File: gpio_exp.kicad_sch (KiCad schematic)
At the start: 23 parts, among them U9 PCA9685PW

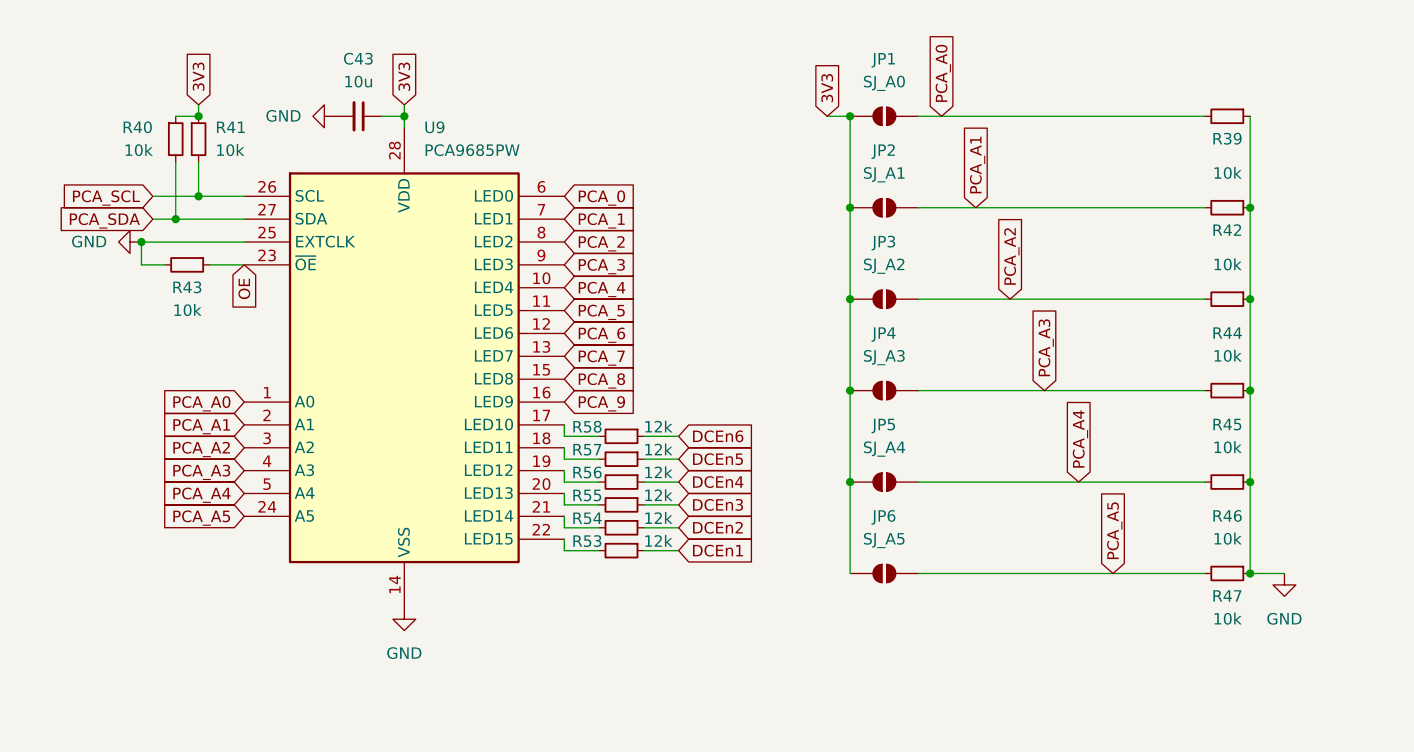
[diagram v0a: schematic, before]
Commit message: gpio expander added comm finished
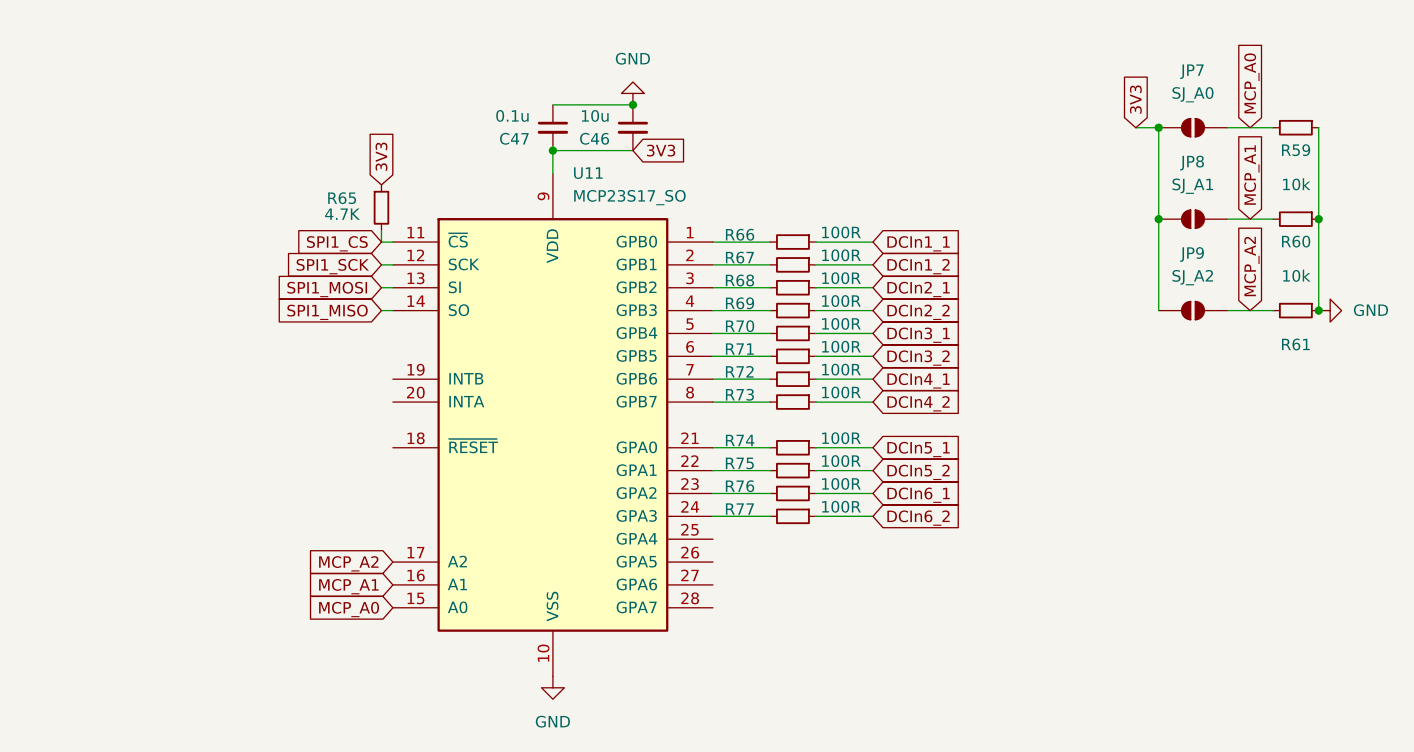
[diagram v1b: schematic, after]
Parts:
- removed C43: 10u, Capacitor_SMD:C_0805_2012Metric, symbol Device:C_Small
- removed JP1: SJ_A0, Jumper:SolderJumper-2_P1.3mm_Open_RoundedPad1.0x1.5mm, symbol Jumper:SolderJumper_2_Open
- removed JP2: SJ_A1, Jumper:SolderJumper-2_P1.3mm_Open_RoundedPad1.0x1.5mm, symbol Jumper:SolderJumper_2_Open
- removed JP3: SJ_A2, Jumper:SolderJumper-2_P1.3mm_Open_RoundedPad1.0x1.5mm, symbol Jumper:SolderJumper_2_Open
- removed JP4: SJ_A3, Jumper:SolderJumper-2_P1.3mm_Open_RoundedPad1.0x1.5mm, symbol Jumper:SolderJumper_2_Open
- removed JP5: SJ_A4, Jumper:SolderJumper-2_P1.3mm_Open_RoundedPad1.0x1.5mm, symbol Jumper:SolderJumper_2_Open
- removed JP6: SJ_A5, Jumper:SolderJumper-2_P1.3mm_Open_RoundedPad1.0x1.5mm, symbol Jumper:SolderJumper_2_Open
- removed R39, R40, R41, R42, R43, R44, R45, R46, R47: 10k, Resistor_SMD:R_0805_2012Metric, symbol Device:R_Small
- removed R53, R54, R55, R56, R57, R58: 12k, Resistor_SMD:R_0805_2012Metric, symbol Device:R_Small
- removed U9: PCA9685PW, Package_SO:TSSOP-28_4.4x9.7mm_P0.65mm, symbol Driver_LED:PCA9685PW
- added C46: 10u, Capacitor_SMD:C_0805_2012Metric, symbol Device:C_Small
- added C47: 0.1u, Capacitor_SMD:C_0805_2012Metric, symbol Device:C_Small
- added JP7: SJ_A0, Jumper:SolderJumper-2_P1.3mm_Open_RoundedPad1.0x1.5mm, symbol Jumper:SolderJumper_2_Open
- added JP8: SJ_A1, Jumper:SolderJumper-2_P1.3mm_Open_RoundedPad1.0x1.5mm, symbol Jumper:SolderJumper_2_Open
- added JP9: SJ_A2, Jumper:SolderJumper-2_P1.3mm_Open_RoundedPad1.0x1.5mm, symbol Jumper:SolderJumper_2_Open
- added R59, R60, R61: 10k, Resistor_SMD:R_0805_2012Metric, symbol Device:R_Small
- added R65: 4.7K, Resistor_SMD:R_0805_2012Metric, symbol Device:R_Small
- added R66, R67, R68, R69, R70, R71, R72, R73, R74, R75, R76, R77: 100R, Resistor_SMD:R_0805_2012Metric, symbol Device:R_Small
- added U11: MCP23S17_SO, Package_SO:SOIC-28W_7.5x17.9mm_P1.27mm, symbol Interface_Expansion:MCP23S17_SO
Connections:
- net 3V3: now also C46.2, C47.2, JP7.1 (A), JP8.1 (A), JP9.1 (A), R65.1, U11.9 (VDD)
- net GND: now also C46.1, C47.1, R59.1, R60.1, R61.1, U11.10 (VSS)
- new net: R73.2, U11.8 (GPB7)
- new net: R70.2, U11.5 (GPB4)
- new net: R66.2, U11.1 (GPB0)
- new net: R67.2, U11.2 (GPB1)
- new net: R74.2, U11.21 (GPA0)
- new net: R75.2, U11.22 (GPA1)
- new net: R76.2, U11.23 (GPA2)
- new net: R77.2, U11.24 (GPA3)
- new net: R68.2, U11.3 (GPB2)
- new net: R69.2, U11.4 (GPB3)
- new net: R71.2, U11.6 (GPB5)
- new net: R72.2, U11.7 (GPB6)
- new net DCIn1_1: R66.1
- new net DCIn1_2: R67.1
- new net DCIn2_1: R68.1
- new net DCIn2_2: R69.1
- new net DCIn3_1: R70.1
- new net DCIn3_2: R71.1
- new net DCIn4_1: R72.1
- new net DCIn4_2: R73.1
- new net DCIn5_1: R74.1
- new net DCIn5_2: R75.1
- new net DCIn6_1: R76.1
- new net DCIn6_2: R77.1
- new net MCP_A0: JP7.2 (B), R59.2, U11.15 (A0)
- new net MCP_A1: JP8.2 (B), R60.2, U11.16 (A1)
- new net MCP_A2: JP9.2 (B), R61.2, U11.17 (A2)
- new net SPI1_CS: R65.2, U11.11 (~{CS})
- new net SPI1_MISO: U11.14 (SO)
- new net SPI1_MOSI: U11.13 (SI)
- new net SPI1_SCK: U11.12 (SCK)

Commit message: Visual Improvements
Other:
- note added: "GPIO Expander"
- note added: "GPIO Expander Address Selection"
- moved on the sheet: C46, C47, JP7, JP8, JP9, R59, R60, R61, R65, R66, R67, R68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

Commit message: schematic finished
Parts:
- added R84: 10K, Resistor_SMD:R_0805_2012Metric, symbol Device:R_Small
- renumbered C47 to C46, C46 to C47, R59 to R68, R65 to R69, R66 to R70, R67 to R71, R60 to R72, R68 to R73, R69 to R74, R70 to R75, R71 to R76, R61 to R77, R72 to R78, R73 to R79, R74 to R80, R75 to R81, R76 to R82, R77 to R83
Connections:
- net 3V3: now also R84.1
- net at U11.18 (~{RESET}): now also R84.2
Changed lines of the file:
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@@
+	(wire
+		(pts
+			(xy 29.21 58.42) (xy 33.02 58.42)
+		)
+		(stroke
+			(width 0)
+			(type default)
+		)
+	)
 	(wire
 		(pts
@@
 		)
 	)
+	(global_label "3V3"
+		(shape input)
+		(at 29.21 53.34 90)
+		(fields_autoplaced yes)
+		(effects
+			(font
+				(size 1.27 1.27)
+			)
+			(justify left)
+		)
+		(property "Intersheetrefs" "${INTERSHEET_REFS}"
+			(at 29.21 46.8472 90)
+			(effects
+				(font
+					(size 1.27 1.27)
+				)
+				(justify left)
+				(hide yes)
+			)
+		)
+	)
 	(global_label "DCIn3_2"
 		(shape input)
@@
 		(on_board yes)
 		(dnp no)
-		(property "Reference" "R73"
+		(property "Reference" "R79"
 			(at 69.85 52.578 90)
 			(effects
@@
 			(project "controllerForVehicle"
 				(path "/f177fb06-71dc-4865-9331-a828b12c2bf7/cf99d41f-154f-4525-9df8-a364b4903864"
-					(reference "R73")
+					(reference "R79")
 					(unit 1)
 				)
@@
 		(on_board yes)
 		(dnp no)
-		(property "Reference" "R70"
+		(property "Reference" "R75"
 			(at 69.85 44.958 90)
 			(effects
@@
 			(project "controllerForVehicle"
 				(path "/f177fb06-71dc-4865-9331-a828b12c2bf7/cf99d41f-154f-4525-9df8-a364b4903864"
-					(reference "R70")
+					(reference "R75")
 					(unit 1)
 				)
@@
 		(dnp no)
 		(fields_autoplaced yes)
-		(property "Reference" "#PWR050"
+		(property "Reference" "#PWR051"
 			(at 50.8 90.17 0)
 			(effects
@@
 			(project "controllerForVehicle"
 				(path "/f177fb06-71dc-4865-9331-a828b12c2bf7/cf99d41f-154f-4525-9df8-a364b4903864"
-					(reference "#PWR050")
+					(reference "#PWR051")
 					(unit 1)
 				)
@@
 		(on_board yes)
 		(dnp no)
-		(property "Reference" "R77"
+		(property "Reference" "R83"
 			(at 69.85 65.278 90)
 			(effects
@@
 			(project "controllerForVehicle"
 				(path "/f177fb06-71dc-4865-9331-a828b12c2bf7/cf99d41f-154f-4525-9df8-a364b4903864"
-					(reference "R77")
+					(reference "R83")
 					(unit 1)
 				)
@@
 		(dnp no)
 		(fields_autoplaced yes)
-		(property "Reference" "C47"
+		(property "Reference" "C46"
 			(at 48.26 24.1365 0)
 			(effects
@@
 			(project "controllerForVehicle"
 				(path "/f177fb06-71dc-4865-9331-a828b12c2bf7/cf99d41f-154f-4525-9df8-a364b4903864"
-					(reference "C47")
+					(reference "C46")
 					(unit 1)
 				)
@@
 		(dnp no)
 		(fields_autoplaced yes)
-		(property "Reference" "C46"
+		(property "Reference" "C47"
 			(at 57.15 24.1365 0)
 			(effects
@@
 			(project "controllerForVehicle"
 				(path "/f177fb06-71dc-4865-9331-a828b12c2bf7/cf99d41f-154f-4525-9df8-a364b4903864"
-					(reference "C46")
+					(reference "C47")
 					(unit 1)
 				)
@@
 		(on_board yes)
 		(dnp no)
-		(property "Reference" "R75"
+		(property "Reference" "R81"
 			(at 69.8482 60.198 90)
 			(effects
@@
 			(project "controllerForVehicle"
 				(path "/f177fb06-71dc-4865-9331-a828b12c2bf7/cf99d41f-154f-4525-9df8-a364b4903864"
-					(reference "R75")
+					(reference "R81")
 					(unit 1)
 				)
@@
 		(on_board yes)
 		(dnp no)
-		(property "Reference" "R68"
+		(property "Reference" "R73"
 			(at 69.85 39.878 90)
 			(effects
@@
 			(project "controllerForVehicle"
 				(path "/f177fb06-71dc-4865-9331-a828b12c2bf7/cf99d41f-154f-4525-9df8-a364b4903864"
-					(reference "R68")
+					(reference "R73")
 					(unit 1)
 				)
@@
 		(on_board yes)
 		(dnp no)
-		(property "Reference" "R74"
+		(property "Reference" "R80"
 			(at 69.85 57.658 90)
 			(effects
@@
 			(project "controllerForVehicle"
 				(path "/f177fb06-71dc-4865-9331-a828b12c2bf7/cf99d41f-154f-4525-9df8-a364b4903864"
-					(reference "R74")
+					(reference "R80")
 					(unit 1)
 				)
@@
 		(on_board yes)
 		(dnp no)
-		(property "Reference" "R72"
+		(property "Reference" "R78"
 			(at 69.85 50.038 90)
 			(effects
@@
 			(project "controllerForVehicle"
 				(path "/f177fb06-71dc-4865-9331-a828b12c2bf7/cf99d41f-154f-4525-9df8-a364b4903864"
-					(reference "R72")
+					(reference "R78")
 					(unit 1)
 				)
@@
 		(on_board yes)
 		(dnp no)
-		(property "Reference" "R71"
+		(property "Reference" "R76"
 			(at 69.85 47.498 90)
 			(effects
@@
 			(project "controllerForVehicle"
 				(path "/f177fb06-71dc-4865-9331-a828b12c2bf7/cf99d41f-154f-4525-9df8-a364b4903864"
-					(reference "R71")
+					(reference "R76")
 					(unit 1)
 				)
@@
 		(on_board yes)
 		(dnp no)
-		(property "Reference" "R61"
+		(property "Reference" "R77"
 			(at 133.35 53.34 90)
 			(effects
@@
 			(project "controllerForVehicle"
 				(path "/f177fb06-71dc-4865-9331-a828b12c2bf7/cf99d41f-154f-4525-9df8-a364b4903864"
-					(reference "R61")
+					(reference "R77")
+					(unit 1)
+				)
+			)
+		)
+	)
+	(symbol
+		(lib_id "Device:R_Small")
+		(at 29.21 55.88 0)
+		(unit 1)
+		(exclude_from_sim no)
+		(in_bom yes)
+		(on_board yes)
+		(dnp no)
+		(property "Reference" "R84"
+			(at 23.114 54.864 0)
+			(effects
+				(font
+					(size 1.27 1.27)
+				)
+				(justify left)
+			)
+		)
+		(property "Value" "10K"
+			(at 23.368 56.896 0)
+			(effects
+				(font
+					(size 1.27 1.27)
+				)
+				(justify left)
+			)
+		)
+		(property "Footprint" "Resistor_SMD:R_0805_2012Metric"
+			(at 29.21 55.88 0)
+			(effects
+				(font
+					(size 1.27 1.27)
+				)
+				(hide yes)
+			)
+		)
+		(property "Datasheet" "~"
+			(at 29.21 55.88 0)
+			(effects
+				(font
+					(size 1.27 1.27)
+				)
+				(hide yes)
+			)
+		)
+		(property "Description" "Resistor, small symbol"
+			(at 29.21 55.88 0)
+			(effects
+				(font
+					(size 1.27 1.27)
+				)
+				(hide yes)
+			)
+		)
+		(pin "1"
+		)
+		(pin "2"
+		)
+		(instances
+			(project "controllerForVehicle"
+				(path "/f177fb06-71dc-4865-9331-a828b12c2bf7/cf99d41f-154f-4525-9df8-a364b4903864"
+					(reference "R84")
 					(unit 1)
 				)
@@
 		(on_board yes)
 		(dnp no)
-		(property "Reference" "R76"
+		(property "Reference" "R82"
 			(at 69.8482 62.738 90)
 			(effects
@@
 			(project "controllerForVehicle"
 				(path "/f177fb06-71dc-4865-9331-a828b12c2bf7/cf99d41f-154f-4525-9df8-a364b4903864"
-					(reference "R76")
+					(reference "R82")
 					(unit 1)
 				)
@@
 		(on_board yes)
 		(dnp no)
-		(property "Reference" "R59"
+		(property "Reference" "R68"
 			(at 133.35 31.75 90)
 			(effects
@@
 			(project "controllerForVehicle"
 				(path "/f177fb06-71dc-4865-9331-a828b12c2bf7/cf99d41f-154f-4525-9df8-a364b4903864"
-					(reference "R59")
+					(reference "R68")
 					(unit 1)
 				)
@@
 		(on_board yes)
 		(dnp no)
-		(property "Reference" "R65"
+		(property "Reference" "R69"
 			(at 25.654 30.734 0)
 			(effects
@@
 			(project "controllerForVehicle"
 				(path "/f177fb06-71dc-4865-9331-a828b12c2bf7/cf99d41f-154f-4525-9df8-a364b4903864"
-					(reference "R65")
+					(reference "R69")
 					(unit 1)
 				)
@@
 		(dnp no)
 		(fields_autoplaced yes)
-		(property "Reference" "#PWR051"
+		(property "Reference" "#PWR050"
 			(at 142.24 49.53 0)
 			(effects
@@
 			(project "controllerForVehicle"
 				(path "/f177fb06-71dc-4865-9331-a828b12c2bf7/cf99d41f-154f-4525-9df8-a364b4903864"
-					(reference "#PWR051")
+					(reference "#PWR050")
 					(unit 1)
 				)
@@
 		(on_board yes)
 		(dnp no)
-		(property "Reference" "R60"
+		(property "Reference" "R72"
 			(at 133.35 41.91 90)
 			(effects
@@
 			(project "controllerForVehicle"
 				(path "/f177fb06-71dc-4865-9331-a828b12c2bf7/cf99d41f-154f-4525-9df8-a364b4903864"
-					(reference "R60")
+					(reference "R72")
 					(unit 1)
 				)
@@
 		(on_board yes)
 		(dnp no)
-		(property "Reference" "R69"
+		(property "Reference" "R74"
 			(at 69.85 42.418 90)
 			(effects
@@
 			(project "controllerForVehicle"
 				(path "/f177fb06-71dc-4865-9331-a828b12c2bf7/cf99d41f-154f-4525-9df8-a364b4903864"
-					(reference "R69")
+					(reference "R74")
 					(unit 1)
 				)
@@
 		(on_board yes)
 		(dnp no)
-		(property "Reference" "R66"
+		(property "Reference" "R70"
 			(at 69.85 34.798 90)
 			(effects
@@
 			(project "controllerForVehicle"
 				(path "/f177fb06-71dc-4865-9331-a828b12c2bf7/cf99d41f-154f-4525-9df8-a364b4903864"
-					(reference "R66")
+					(reference "R70")
 					(unit 1)
 				)
@@
 		(on_board yes)
 		(dnp no)
-		(property "Reference" "R67"
+		(property "Reference" "R71"
 			(at 69.85 37.338 90)
 			(effects
@@
 			(project "controllerForVehicle"
 				(path "/f177fb06-71dc-4865-9331-a828b12c2bf7/cf99d41f-154f-4525-9df8-a364b4903864"
-					(reference "R67")
-					(unit 1)
-				)
+					(reference "R71")
+					(unit 1)
+				)

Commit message: dc sürücü yol çizimleri yapıldı
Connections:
- net DCIn1_1: now also R79.1; no longer R70.1
- net DCIn1_2: now also R78.1; no longer R71.1
- net DCIn2_1: now also R76.1; no longer R73.1
- net DCIn2_2: now also R75.1; no longer R74.1
- net DCIn3_1: now also R74.1; no longer R75.1
- net DCIn3_2: now also R73.1; no longer R76.1
- net DCIn4_1: now also R71.1; no longer R78.1
- net DCIn4_2: now also R70.1; no longer R79.1

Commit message: Routing
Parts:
- removed R70, R71, R73, R74, R75, R76, R78, R79, R80, R81, R82, R83: 100R, Resistor_SMD:R_0805_2012Metric, symbol Device:R_Small
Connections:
- net DCIn1_1: now also U11.21 (GPA0)
- net DCIn1_2: now also U11.22 (GPA1)
- net DCIn2_1: now also U11.23 (GPA2)
- net DCIn2_2: now also U11.24 (GPA3)
- net DCIn3_1: now also U11.8 (GPB7)
- net DCIn3_2: now also U11.7 (GPB6)
- net DCIn4_1: now also U11.6 (GPB5)
- net DCIn4_2: now also U11.5 (GPB4)
- net DCIn5_1: now also U11.4 (GPB3)
- net DCIn5_2: now also U11.3 (GPB2)
- net DCIn6_1: now also U11.2 (GPB1)
- net DCIn6_2: now also U11.1 (GPB0)
